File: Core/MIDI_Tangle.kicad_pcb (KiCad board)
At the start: 2 copper layers, 40 x 97.5 mm, 82 parts, among them J1 USB_C_Receptacle_USB2.0, J2 Conn_01x04, J21 Conn_02x08_Odd_Even, J4 Conn_01x06_Male, J5 Conn_01x08_Female, J6 Conn_01x08_Female, J7 Conn_01x08_Female, J8 Conn_01x08_Female, SW1 SW_Push_DPDT, U1 ATSAMD21G15B-A, U10 TL072, U11 TL072, U12 TL072, U13 TL072, U14 MCP2517FD-xSL, U15 TLE9250V, U18 MIC5504-3.3YM5, U2 DG408, U3 DG408, U4 DG408, U5 DG408, U6 DG408, U7 DG408, U8 DG408, U9 DG408, Y1 20MHz

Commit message: Fix DRC errors
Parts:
- moved R7 0.57 mm to (170.4, 73.3)
- moved C37 0.54 mm to (176.5, 65.8)
- moved C41 0.51 mm to (176.0, 57.2)
- moved R11 0.51 mm to (172.8, 58.0)
- moved R12 0.51 mm to (172.8, 56.5)
- moved C39 0.31 mm to (190.0, 59.9)
- moved C33 0.28 mm to (182.8, 81.0)
- moved C40 0.26 mm to (191.3, 61.2)
- moved J4 0.25 mm to (166.9, 75.4)
- moved R2 0.25 mm to (189.0, 68.6)
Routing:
- net Net-(R11-Pad2): track 1.74 -> 2.50 mm

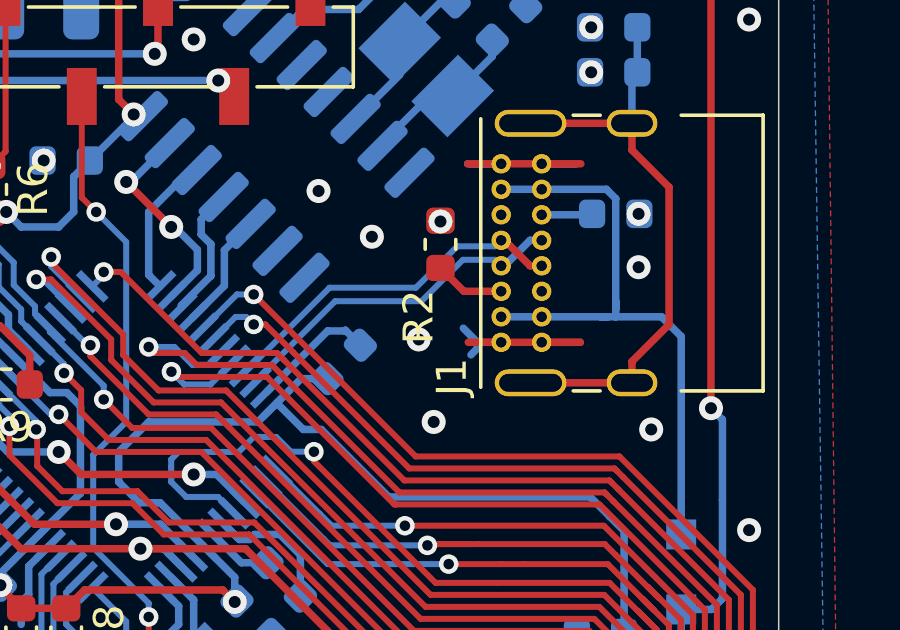
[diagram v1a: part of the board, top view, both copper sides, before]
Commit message: Add custom footprints and symbols
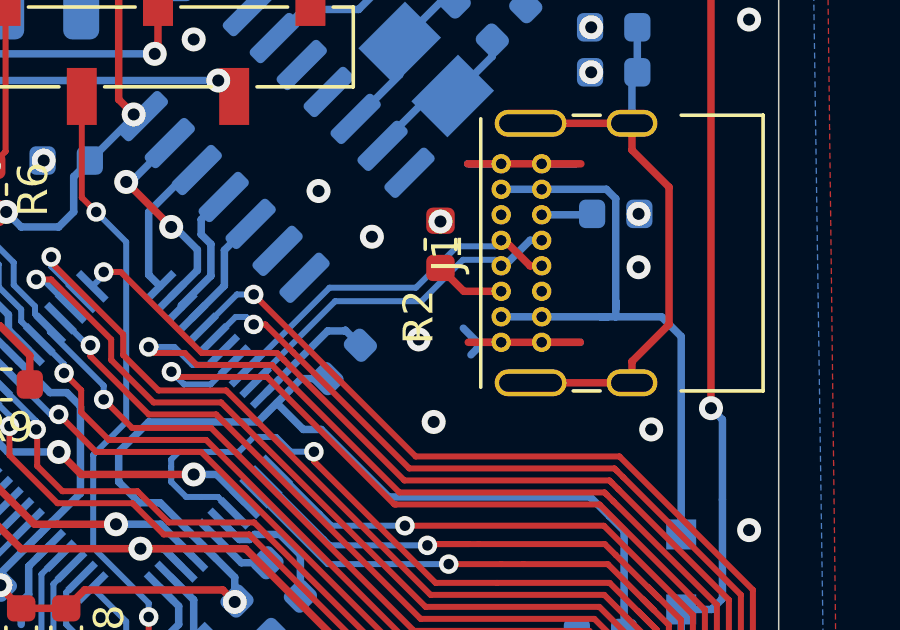
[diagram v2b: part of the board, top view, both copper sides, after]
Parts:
- C3: value 100nF -> 1µF
- C41: value 22nF -> 4.7nF
- J1: footprint CustomLib:USB_C_Receptacle_GCT_USB4085_Slimmed -> Custom_FP:USB_C_Receptacle_GCT_USB4085_Slimmed
- J2: footprint CustomLib:MicroMatch_04_Vertical_SMD -> Custom_FP:MicroMatch_04_Vertical_SMD
- J21: footprint CustomLib:Header_2x8_Shrouded_SMD -> Custom_FP:Header_2x8_Shrouded_SMD
- R11, R12: value 120 -> 56
- SW1: footprint CustomLib:SlideDPDT_JS202011 -> Custom_FP:SlideDPDT_JS202011
- Y1: footprint CustomLib:Crystal_2pin_2.0x2.5mm -> Custom_FP:Crystal_2pin_2.0x2.5mm
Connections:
- J1 pad A8: (no net) -> Net-(J1-PadA8)
- J1 pad B8: (no net) -> Net-(J1-PadB8)
- J21 pad 13: (no net) -> Net-(J21-Pad13)
- J21 pad 14: (no net) -> Net-(J21-Pad14)
- J21 pad 15: (no net) -> Net-(J21-Pad15)
- J21 pad 16: (no net) -> Net-(J21-Pad16)
- J4 pad 6: (no net) -> Net-(J4-Pad6)
- SW1 pad 3: (no net) -> Net-(SW1-Pad3)
- SW1 pad 6: (no net) -> Net-(SW1-Pad6)
- U14 pad 3: (no net) -> Net-(U14-Pad3)
- U14 pad 4: (no net) -> Net-(U14-Pad4)
- U14 pad 8: (no net) -> Net-(U14-Pad8)
- U14 pad 9: (no net) -> Net-(U14-Pad9)
- U18 pad 4: (no net) -> Net-(U18-Pad4)

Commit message: Update PCB layout
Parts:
- added C42: 100nF, Capacitor_SMD:C_0603_1608Metric, F.Cu at (183.6, 69.2)
- added C43: 100nF, Capacitor_SMD:C_0603_1608Metric, F.Cu at (197.8, 113.2)
- added C44: 100nF, Capacitor_SMD:C_0603_1608Metric, F.Cu at (197.9, 95.7)
- added C45: 100nF, Capacitor_SMD:C_0603_1608Metric, F.Cu at (197.9, 127.8)
- added Q1: BSS84, Package_TO_SOT_SMD:SOT-23, B.Cu at (182.0, 115.2)
- added Q2: 2N7002, Package_TO_SOT_SMD:SOT-23, B.Cu at (172.2, 115.2)
- added Q3: BSS84, Package_TO_SOT_SMD:SOT-23, B.Cu at (196.3, 89.8)
- added R10: 10k, Resistor_SMD:R_0603_1608Metric, B.Cu at (171.4, 72.3)
- added R13: 1M, Resistor_SMD:R_0603_1608Metric, F.Cu at (195.3, 85.0)
- added SW2: SW_SPST, Custom_FP:Tactile_angled_5x5.4_SMD, F.Cu at (164.8, 78.9)
- added SW3: SW_SPST, Custom_FP:Tactile_angled_5x5.4_SMD, F.Cu at (164.8, 70.9)
- added U16: CAT250xxx, Package_SO:SO-8_3.9x4.9mm_P1.27mm, F.Cu at (178.4, 71.1)
- added U17: 74HC595, Package_SO:SO-16_3.9x9.9mm_P1.27mm, F.Cu at (195.3, 102.4)
- added U19: 74HC595, Package_SO:SO-16_3.9x9.9mm_P1.27mm, F.Cu at (195.3, 120.0)
- added U20: 74HC595, Package_SO:SO-16_3.9x9.9mm_P1.27mm, F.Cu at (195.3, 134.5)
- J1: footprint Custom_FP:USB_C_Receptacle_GCT_USB4085_Slimmed -> Connector_USB:USB_C_Receptacle_HRO_TYPE-C-31-M-12
- J2: footprint Custom_FP:MicroMatch_04_Vertical_SMD -> Custom_FP:MicroMatch_04_Vertical_SMD_Lock
- J4: footprint Connector_PinHeader_2.54mm:PinHeader_2x03_P2.54mm_Vertical_SMD -> Custom_FP:TSM103-DH
- R11, R12: value 56 -> 62
- R3, R7: moved to F.Cu
- moved J4 25.8 mm to (192.4, 79.0), turned to 180 degrees
- moved R7 8.17 mm to (172.1, 81.3), turned to -135 degrees
- moved R5 6.06 mm to (178.1, 66.9)
- moved R9 5.88 mm to (177.2, 78.5), turned to 90 degrees
- moved J1 5.69 mm to (196.0, 69.1)
- moved R6 5.58 mm to (179.6, 66.9)
- moved R3 5.03 mm to (189.9, 66.7), turned to -90 degrees
- moved D14 4.73 mm to (197.0, 84.2)
- moved C17 3.65 mm to (184.6, 118.7), turned to -90 degrees
- moved C35 3.40 mm to (173.9, 112.2)
- moved C34 3.38 mm to (181.1, 112.1)
- moved R2 3.18 mm to (189.9, 71.6), turned to 90 degrees
- moved C18 2.89 mm to (175.7, 121.0)
- moved U12 2.55 mm to (180.2, 119.8)
- moved C1 2.40 mm to (197.0, 62.2), turned to 90 degrees
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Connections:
- net MIDIBUS+ renamed M2IDI+
- net MIDIBUS- renamed M2IDI-
- J1 pad A8: Net-(J1-PadA8) -> unconnected-(J1-SBU1-PadA8)
- J1 pad B8: Net-(J1-PadB8) -> unconnected-(J1-SBU2-PadB8)
- J21 pad 1: -VDC -> Net-(J21-Pin_1)
- J21 pad 10: +VDC -> Net-(J21-Pin_10)
- J21 pad 11: +5V -> Net-(J21-Pin_11)
- J21 pad 12: +5V -> Net-(J21-Pin_11)
- J21 pad 13: Net-(J21-Pad13) -> unconnected-(J21-Pin_13-Pad13)
- J21 pad 14: Net-(J21-Pad14) -> unconnected-(J21-Pin_14-Pad14)
- J21 pad 15: Net-(J21-Pad15) -> unconnected-(J21-Pin_15-Pad15)
- J21 pad 16: Net-(J21-Pad16) -> unconnected-(J21-Pin_16-Pad16)
- J21 pad 2: -VDC -> Net-(J21-Pin_1)
- J21 pad 9: +VDC -> Net-(J21-Pin_10)
- J4 pad 2: LED -> SWDIO
- J4 pad 6: Net-(J4-Pad6) -> unconnected-(J4-Pin_6-Pad6)
- J5 pad 3: Butt_A -> Out1
- J5 pad 4: Butt_B -> Out2
- J5 pad 5: Butt_X -> Butt_A
- J5 pad 6: Out2 -> Butt_B
- J5 pad 7: Out1 -> GND
- J6 pad 5: Butt_X -> Out4
- J6 pad 6: Out4 -> Butt_X
- J6 pad 8: GND -> LED
- J7 pad 3: Butt_A -> GND
- J7 pad 4: Butt_B -> GND
- J7 pad 8: LED -> GND
- J8 pad 3: Butt_C -> GND
- J8 pad 4: Butt_D -> GND
- J8 pad 5: Butt_Y -> GND
- SW1 pad 3: Net-(SW1-Pad3) -> unconnected-(SW1-C-Pad3)
- SW1 pad 6: Net-(SW1-Pad6) -> unconnected-(SW1-C-Pad6)
- U1 pad 1: M20 -> unconnected-(U1-PA00-Pad1)
- U1 pad 10: M30 -> unconnected-(U1-PA05-Pad10)
- U1 pad 11: M02 -> unconnected-(U1-PA06-Pad11)
- U1 pad 12: M01 -> unconnected-(U1-PA07-Pad12)
- U1 pad 13: M00 -> PROG
- U1 pad 14: M12 -> unconnected-(U1-PA09-Pad14)
- U1 pad 15: M11 -> unconnected-(U1-PA10-Pad15)
- U1 pad 16: M10 -> unconnected-(U1-PA11-Pad16)
- U1 pad 2: M21 -> unconnected-(U1-PA01-Pad2)
- U1 pad 21: M40 -> EEPROM_MISO
- U1 pad 22: M42 -> EEPROM_CS
- U1 pad 23: M41 -> EEPROM_MOSI
- U1 pad 24: M61 -> EEPROM_SCK
- U1 pad 29: M60 -> unconnected-(U1-PA20-Pad29)
- U1 pad 30: M62 -> unconnected-(U1-PA21-Pad30)
- U1 pad 31: M70 -> unconnected-(U1-PA22-Pad31)
- U1 pad 32: M72 -> unconnected-(U1-PA23-Pad32)
- U1 pad 37: M71 -> Shiftreg_Data
- U1 pad 38: M51 -> Shiftreg_Clk
- U1 pad 39: M52 -> Shiftreg_strobe
- U1 pad 41: M50 -> LED
- U1 pad 46: LED -> SWDIO
- U1 pad 7: M22 -> unconnected-(U1-PB08-Pad7)
- U1 pad 8: M32 -> unconnected-(U1-PB09-Pad8)
- U1 pad 9: M31 -> unconnected-(U1-PA04-Pad9)
- U14 pad 3: Net-(U14-Pad3) -> unconnected-(U14-CLKO/SOF-Pad3)
- U14 pad 4: Net-(U14-Pad4) -> unconnected-(U14-~{INT}-Pad4)
- U14 pad 8: Net-(U14-Pad8) -> unconnected-(U14-~{INT1}/GPIO1-Pad8)
- U14 pad 9: Net-(U14-Pad9) -> unconnected-(U14-~{INT0}/GPIO0/XSTBY-Pad9)
- U18 pad 4: Net-(U18-Pad4) -> unconnected-(U18-NC-Pad4)
- U2 pad 1: M00 -> A00
- U2 pad 10: In2 -> In7
- U2 pad 11: In8 -> In6
- U2 pad 12: In6 -> In5
- U2 pad 15: M02 -> A02
- U2 pad 16: M01 -> A01
- U2 pad 4: In5 -> In1
- U2 pad 5: In7 -> In2
- U2 pad 6: In1 -> In3
- U2 pad 7: In3 -> In4
- U2 pad 9: In4 -> In8
- U3 pad 1: M10 -> A10
- U3 pad 10: In2 -> In7
- U3 pad 11: In8 -> In6
- U3 pad 12: In6 -> In5
- U3 pad 15: M12 -> A12
- U3 pad 16: M11 -> A11
- U3 pad 4: In5 -> In1
- U3 pad 5: In7 -> In2
- U3 pad 6: In1 -> In3
- U3 pad 7: In3 -> In4
- U3 pad 9: In4 -> In8
- U4 pad 1: M20 -> A20
- U4 pad 10: In2 -> In7
- U4 pad 11: In8 -> In6
- U4 pad 12: In6 -> In5
- U4 pad 15: M22 -> A22
- U4 pad 16: M21 -> A21
- U4 pad 4: In5 -> In1
- U4 pad 5: In7 -> In2
- U4 pad 6: In1 -> In3
- U4 pad 7: In3 -> In4
- U4 pad 9: In4 -> In8
- U5 pad 1: M30 -> A30
- U5 pad 10: In2 -> In7
- U5 pad 11: In8 -> In6
- U5 pad 12: In6 -> In5
- U5 pad 15: M32 -> A32
- U5 pad 16: M31 -> A31
- U5 pad 4: In5 -> In1
- U5 pad 5: In7 -> In2
- U5 pad 6: In1 -> In3
- U5 pad 7: In3 -> In4
- U5 pad 9: In4 -> In8
- U6 pad 1: M40 -> A40
- U6 pad 10: In6 -> In7
- U6 pad 11: In4 -> In6
- U6 pad 12: In2 -> In5
- U6 pad 15: M42 -> A42
- U6 pad 16: M41 -> A41
- U6 pad 5: In3 -> In2
- U6 pad 6: In5 -> In3
- U6 pad 7: In7 -> In4
- U7 pad 1: M50 -> A50
- U7 pad 10: In6 -> In7
- U7 pad 11: In4 -> In6
- U7 pad 12: In2 -> In5
- U7 pad 15: M52 -> A52
- U7 pad 16: M51 -> A51
- U7 pad 5: In3 -> In2
- U7 pad 6: In5 -> In3
- U7 pad 7: In7 -> In4
- U8 pad 1: M60 -> A60
- U8 pad 10: In6 -> In7
- U8 pad 11: In4 -> In6
- U8 pad 12: In2 -> In5
- U8 pad 15: M62 -> A62
- U8 pad 16: M61 -> A61
- U8 pad 5: In3 -> In2
- U8 pad 6: In5 -> In3
- U8 pad 7: In7 -> In4
- U9 pad 1: M70 -> A70
- U9 pad 10: In6 -> In7
- U9 pad 11: In4 -> In6
- U9 pad 12: In2 -> In5
- U9 pad 15: M72 -> A72
- U9 pad 16: M71 -> A71
- U9 pad 5: In3 -> In2
- U9 pad 6: In5 -> In3
- U9 pad 7: In7 -> In4
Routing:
- net M72: track 105.9 -> 0.00 mm, vias 2 -> 0
- net M70: track 102.6 -> 0.00 mm, vias 2 -> 0
- net M51: track 101.3 -> 0.00 mm, vias 3 -> 0
- net M50: track 100.0 -> 0.00 mm, vias 3 -> 0
- net M52: track 99.0 -> 0.00 mm, vias 3 -> 0
- net M42: track 97.9 -> 0.00 mm, vias 3 -> 0
- net M61: track 96.8 -> 0.00 mm, vias 2 -> 0
- net M71: track 96.2 -> 0.00 mm, vias 2 -> 0
- net M41: track 95.9 -> 0.00 mm, vias 3 -> 0
- net M62: track 93.8 -> 0.00 mm, vias 2 -> 0
- net M60: track 90.3 -> 0.00 mm, vias 2 -> 0
- net Butt_C: track 95.5 -> 11.5 mm, vias 5 -> 2
- net M40: track 82.4 -> 0.00 mm, vias 3 -> 0
- net Butt_D: track 87.5 -> 8.43 mm, vias 5 -> 1
- net +3V3: track 91.6 -> 168.7 mm, vias 7 -> 13
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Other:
- net class Default removed
- net class Signal removed
- board text added: "M2IDI_Tangle V1.1 GuavTek"
- board text removed: "MIDIBUS_Tangle V1.0 GuavTek"
